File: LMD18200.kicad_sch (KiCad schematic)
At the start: 5 parts, among them J4 Conn_01x02_Socket, U2 LMD18200

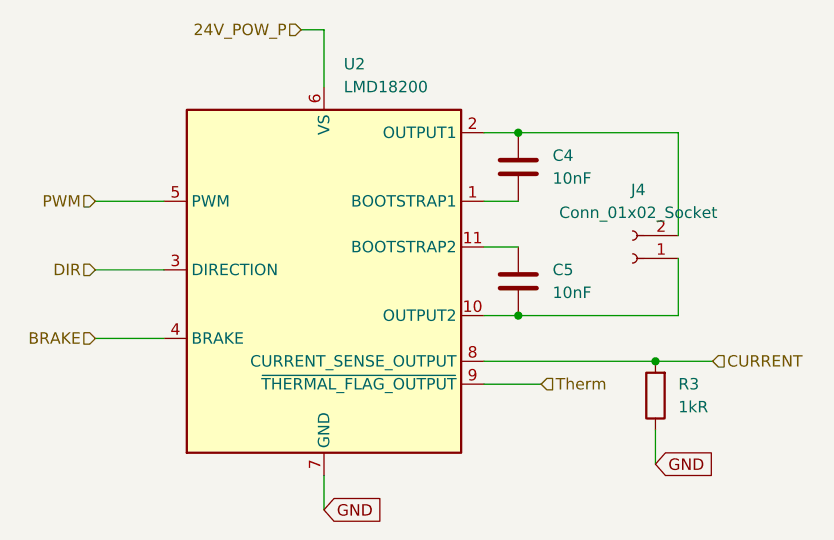
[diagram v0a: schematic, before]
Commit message: Add option 12V Elec + add missing brake pullups
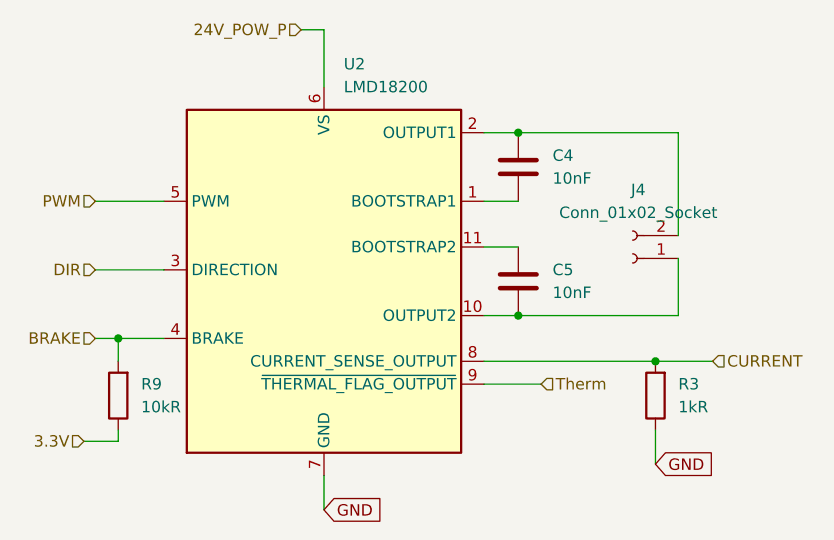
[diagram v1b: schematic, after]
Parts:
- added R9: 10kR, Resistor_SMD:R_0603_1608Metric, symbol Device:R
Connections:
- net BRAKE: now also R9.2
- new net 3.3V: R9.1
